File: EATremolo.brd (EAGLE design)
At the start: 54 x 39.4 mm, 34 parts, among them Q1 2N5457, Q2 2N3904, Q3 2N5457, Q4 2N5088

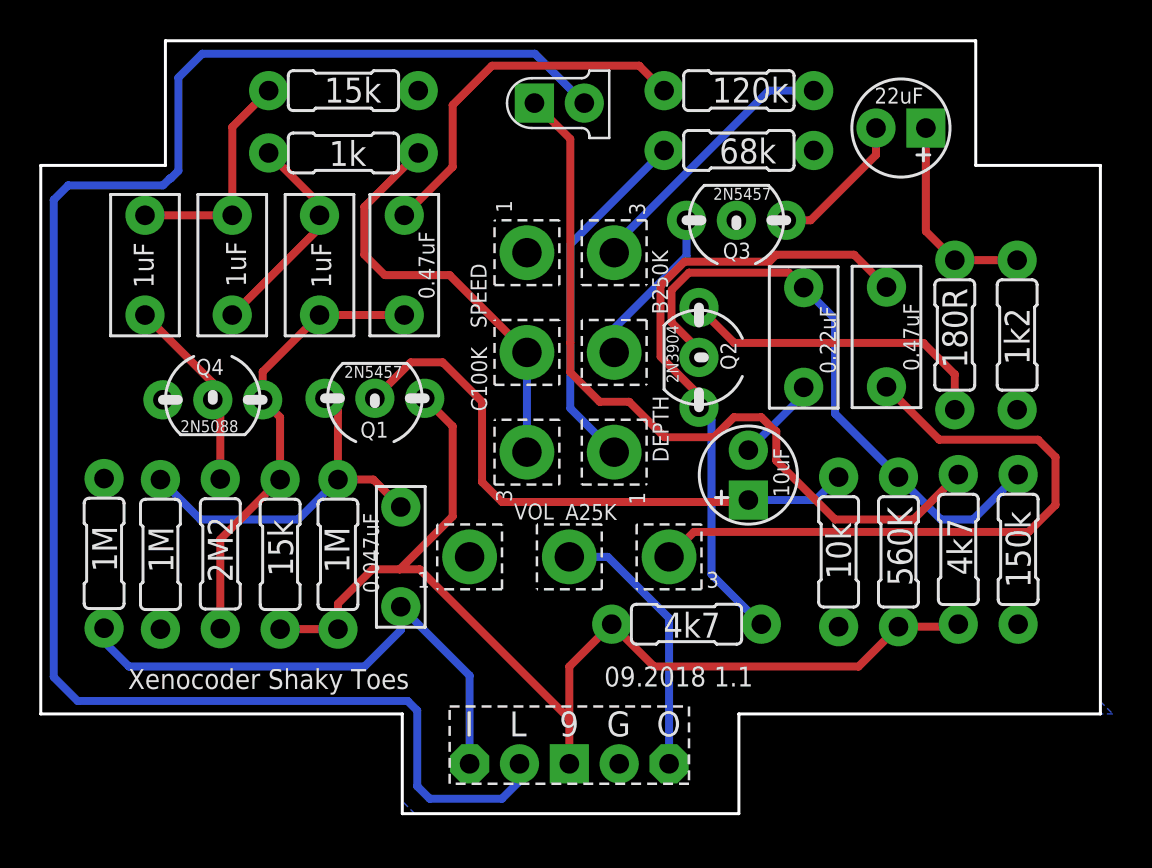
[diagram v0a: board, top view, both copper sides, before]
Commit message: Fixed issue where speed pot was wired (and laid out) backwards
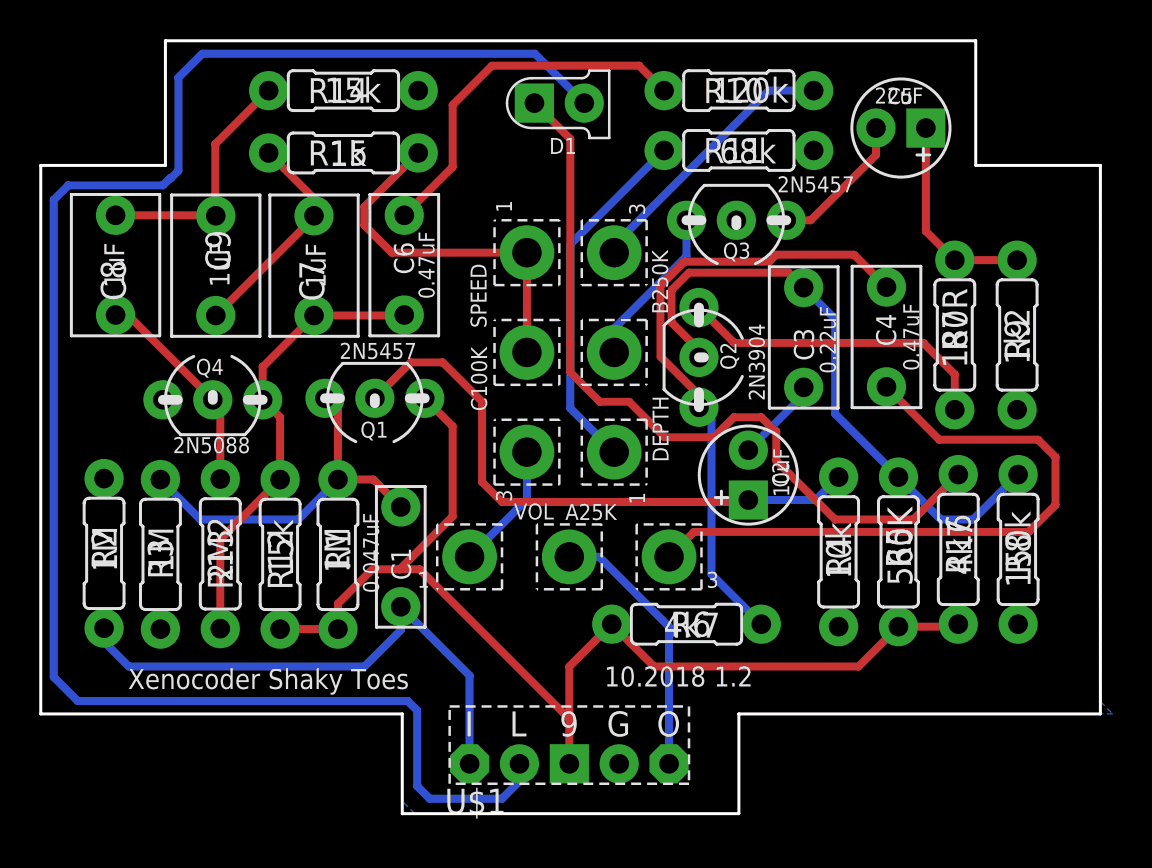
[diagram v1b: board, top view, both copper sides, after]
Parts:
- C7, C8, C9: device mb_caps-box:072X035 -> mb_caps-box:072X045
- moved C8 1.50 mm to (3.81, 27.9)
- moved C9 0.84 mm to (8.92, 27.9)
- moved C7 0.28 mm to (13.9, 27.9)
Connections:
- net GND: now also SPEED.3; no longer SPEED.1
- net N$19: now also SPEED.1; no longer SPEED.3
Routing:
- net GND: track 0.00 -> 6.54 mm
- net N$19: track 21.7 -> 18.8 mm
- net N$18: track 11.6 -> 12.6 mm
- net N$16: track 9.95 -> 10.9 mm
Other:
- board text added: "10.2018 1.2"
- board text removed: "09.2018 1.1"

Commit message: Updated MMBF5457 to right footprint
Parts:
- added U$2, U$3: MMBF5457, xc_library:SOT23
- moved Q3 4.55 mm to (40.0, 30.5)
- moved Q1 3.66 mm to (20.6, 20.5), turned to 90 degrees
- moved Q4 3.00 mm to (5.77, 21.1)
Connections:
- net GND: now also U$3.1
- net N$11: now also U$3.3
- net N$2: now also U$2.3
- net N$22: now also U$2.1
- net N$4: now also U$2.2
- net N$9: now also U$3.2
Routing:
- net GND: track 6.54 -> 17.5 mm
- net N$11: track 8.26 -> 16.4 mm
- net N$2: track 18.9 -> 25.7 mm
- net N$9: track 7.32 -> 13.0 mm
- net N$22: track 57.8 -> 63.0 mm
- net N$15: track 23.3 -> 26.5 mm
- net N$4: track 30.2 -> 28.8 mm

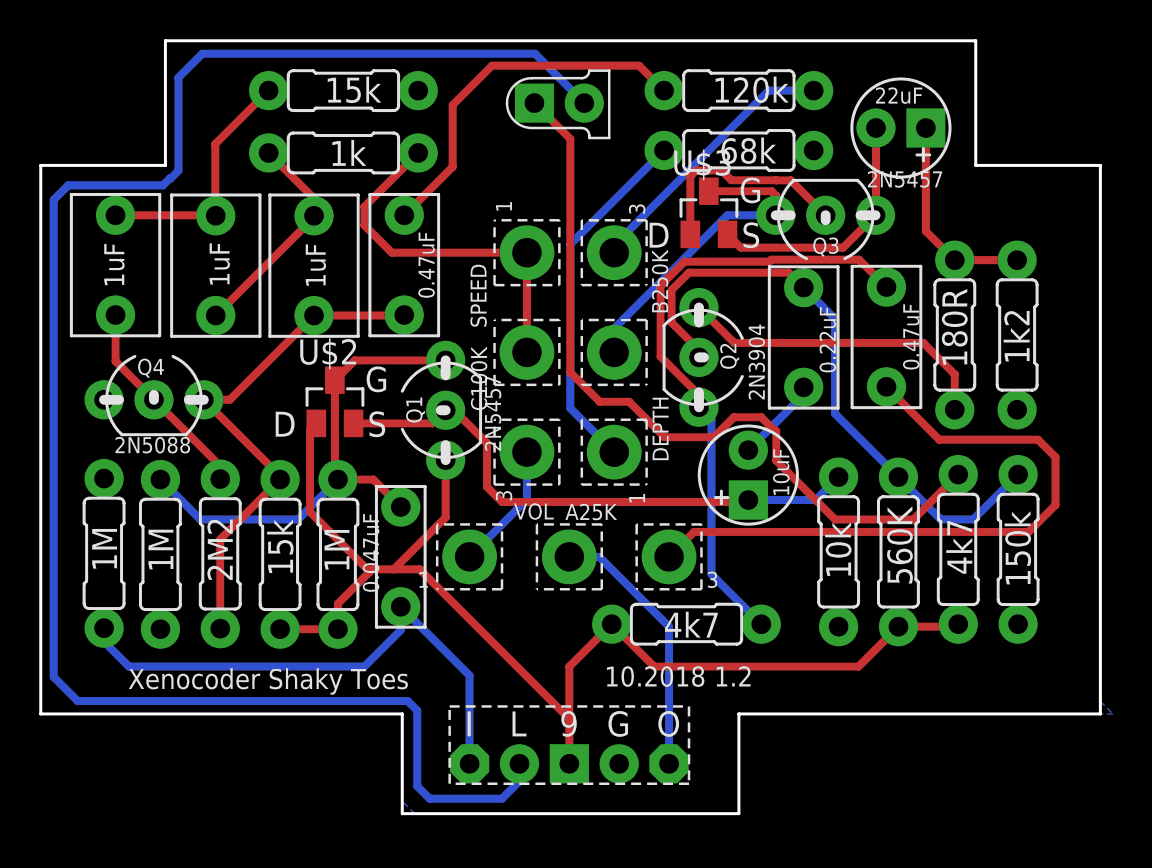
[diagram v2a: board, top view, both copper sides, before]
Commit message: Fixed issue with SMD 5457
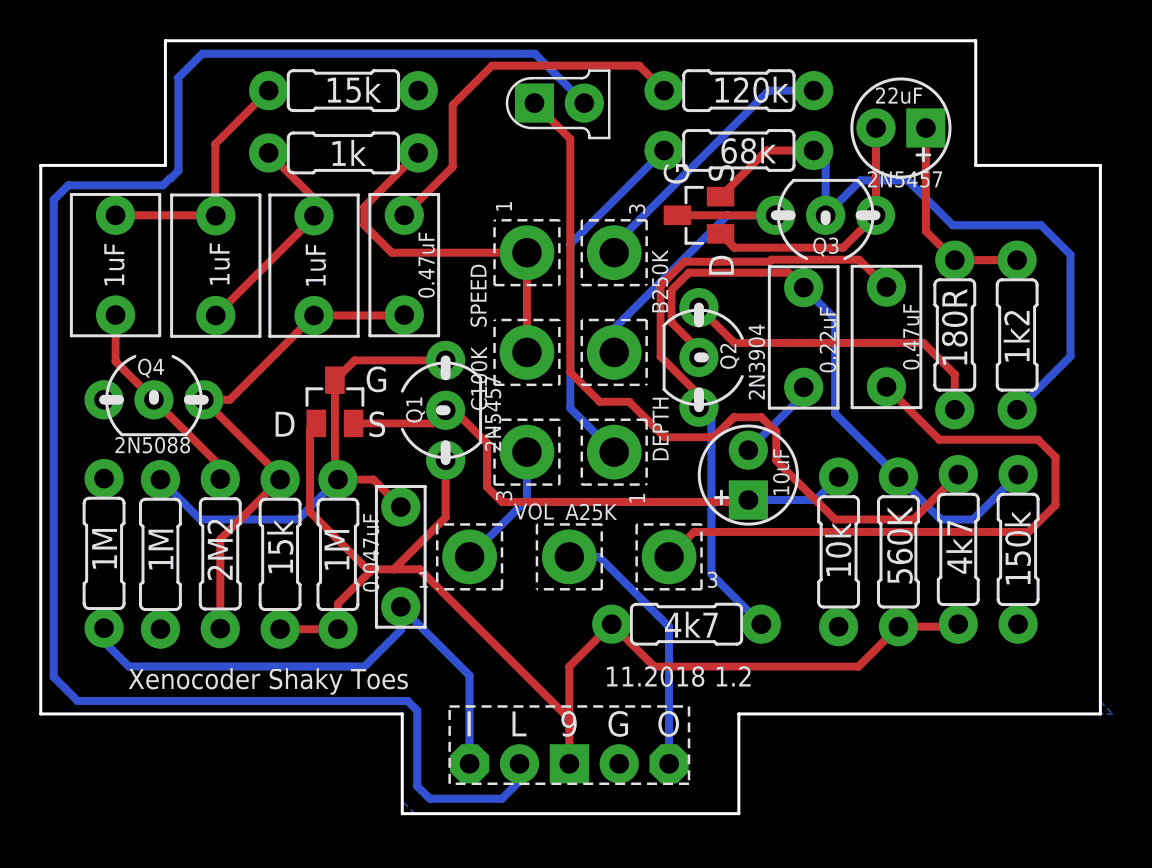
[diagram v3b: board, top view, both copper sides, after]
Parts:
- moved U$3 0.52 mm to (33.5, 30.5), turned to 90 degrees
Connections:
- net GND: now also U$3.2; no longer U$3.1
- net N$9: now also U$3.1; no longer U$3.2
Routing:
- net GND: track 17.5 -> 39.6 mm
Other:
- board text added: "11.2018 1.2"
- board text removed: "10.2018 1.2"
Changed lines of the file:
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@@
 <plain>
 <text x="4.445" y="6.35" size="1.016" layer="25" font="vector">Xenocoder Shaky Toes</text>
-<text x="28.702" y="6.477" size="1.016" layer="25" font="vector">10.2018 1.2</text>
+<text x="28.702" y="6.477" size="1.016" layer="25" font="vector">11.2018 1.2</text>
 <wire x1="0" y1="5.08" x2="18.415" y2="5.08" width="0.1524" layer="20"/>
 <wire x1="18.415" y1="5.08" x2="18.415" y2="0" width="0.1524" layer="20"/>
@@
 <element name="U$1" library="xc_library" package="BOARDLINK" value="BOARDLINK" x="24.384" y="2.54" smashed="yes"/>
 <element name="U$2" library="xc_library" package="SOT23" value="MMBF5457" x="14.986" y="20.9804" smashed="yes">
-<attribute name="NAME" x="13.081" y="22.8854" size="1.27" layer="25"/>
-<attribute name="VALUE" x="13.081" y="17.8054" size="1.27" layer="27"/>
-</element>
-<element name="U$3" library="xc_library" package="SOT23" value="MMBF5457" x="34.036" y="30.607" smashed="yes">
-<attribute name="NAME" x="32.131" y="32.512" size="1.27" layer="25"/>
-<attribute name="VALUE" x="32.131" y="27.432" size="1.27" layer="27"/>
+<attribute name="VALUE" x="10.16" y="22.8854" size="1.27" layer="27"/>
+</element>
+<element name="U$3" library="xc_library" package="SOT23" value="MMBF5457" x="33.528" y="30.48" smashed="yes" rot="R90">
+<attribute name="VALUE" x="32.258" y="32.385" size="1.27" layer="27" rot="R180"/>
 </element>
 </elements>
@@
 <wire x1="21.844" y1="13.081" x2="24.765" y2="16.002" width="0.4064" layer="16"/>
 <wire x1="24.765" y1="16.002" x2="24.765" y2="18.415" width="0.4064" layer="16"/>
-<contactref element="U$3" pad="1"/>
-<wire x1="39.9796" y1="30.48" x2="38.2016" y2="32.258" width="0.4064" layer="1"/>
-<wire x1="38.2016" y1="32.258" x2="37.46786875" y2="32.258" width="0.4064" layer="1"/>
-<wire x1="37.46006875" y1="32.2658" x2="35.179" y2="32.2658" width="0.4064" layer="1"/>
-<wire x1="37.46786875" y1="32.258" x2="37.46006875" y2="32.2658" width="0.4064" layer="1"/>
-<wire x1="34.8916" y1="32.55429375" x2="34.68329375" y2="32.7626" width="0.4064" layer="1"/>
-<wire x1="34.68329375" y1="32.7626" x2="33.38870625" y2="32.7626" width="0.4064" layer="1"/>
-<wire x1="35.179" y1="32.2658" x2="34.8916" y2="32.5532" width="0.4064" layer="1"/>
-<wire x1="34.8916" y1="32.5532" x2="34.8916" y2="32.55429375" width="0.4064" layer="1"/>
-<wire x1="33.38870625" y1="32.7626" x2="33.086" y2="32.45989375" width="0.4064" layer="1"/>
-<wire x1="33.086" y1="32.45989375" x2="33.086" y2="29.507" width="0.4064" layer="1"/>
+<contactref element="U$3" pad="2"/>
+<wire x1="39.9796" y1="30.48" x2="39.9796" y2="33.1724" width="0.4064" layer="16"/>
+<wire x1="39.9796" y1="33.1724" x2="39.37" y2="33.782" width="0.4064" layer="16"/>
+<wire x1="39.9796" y1="30.48" x2="41.7576" y2="32.258" width="0.4064" layer="16"/>
+<wire x1="44.1706" y1="32.258" x2="46.4566" y2="29.972" width="0.4064" layer="16"/>
+<wire x1="50.9524" y1="29.972" x2="52.451" y2="28.4734" width="0.4064" layer="16"/>
+<wire x1="52.451" y1="23.2918" x2="49.7332" y2="20.574" width="0.4064" layer="16"/>
+<wire x1="41.7576" y1="32.258" x2="44.1706" y2="32.258" width="0.4064" layer="16"/>
+<wire x1="46.4566" y1="29.972" x2="50.9524" y2="29.972" width="0.4064" layer="16"/>
+<wire x1="52.451" y1="28.4734" x2="52.451" y2="23.2918" width="0.4064" layer="16"/>
+<wire x1="34.628" y1="31.43" x2="36.98" y2="33.782" width="0.4064" layer="1"/>
+<wire x1="36.98" y1="33.782" x2="39.37" y2="33.782" width="0.4064" layer="1"/>
 </signal>
 <signal name="N$5">
@@
 <contactref element="C5" pad="-"/>
 <contactref element="Q3" pad="3"/>
-<contactref element="U$3" pad="2"/>
 <wire x1="42.545" y1="34.925" x2="42.545" y2="30.5054" width="0.4064" layer="1"/>
 <wire x1="42.545" y1="30.5054" x2="42.5196" y2="30.48" width="0.4064" layer="1"/>
-<wire x1="34.986" y1="29.507" x2="35.664" y2="28.829" width="0.4064" layer="1"/>
+<contactref element="U$3" pad="1"/>
+<wire x1="34.628" y1="29.53" x2="35.329" y2="28.829" width="0.4064" layer="1"/>
 <wire x1="40.8686" y1="28.829" x2="42.5196" y2="30.48" width="0.4064" layer="1"/>
-<wire x1="35.664" y1="28.829" x2="40.8686" y2="28.829" width="0.4064" layer="1"/>
+<wire x1="35.329" y1="28.829" x2="40.8686" y2="28.829" width="0.4064" layer="1"/>
 </signal>
 <signal name="N$14">
@@
 <wire x1="29.21" y1="24.7142" x2="34.9758" y2="30.48" width="0.4064" layer="16"/>
 <contactref element="U$3" pad="3"/>
-<wire x1="34.036" y1="31.707" x2="37.2286" y2="31.707" width="0.4064" layer="1"/>
-<wire x1="37.2286" y1="31.707" x2="37.465" y2="31.4706" width="0.4064" layer="1"/>
-<wire x1="37.465" y1="31.4706" x2="37.4396" y2="31.4452" width="0.4064" layer="1"/>
-<wire x1="37.4396" y1="31.4452" x2="37.4396" y2="30.48" width="0.4064" layer="1"/>
+<wire x1="32.428" y1="30.48" x2="37.4396" y2="30.48" width="0.4064" layer="1"/>
 </signal>
 <signal name="N$12">

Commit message: Version 1.0 of Tremolo Thing
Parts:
- C1: value 0.047uF -> 47nF
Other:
- board text added: "2020.04 v1.0"
- board text added: "Xenocoder Tremolo Thing"
- board text removed: "11.2018 1.2"
- board text removed: "Xenocoder Shaky Toes"
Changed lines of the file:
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@@
 <?xml version="1.0" encoding="utf-8"?>
 <!DOCTYPE eagle SYSTEM "eagle.dtd">
-<eagle version="9.2.2">
+<eagle version="9.5.2">
 <drawing>
 <settings>
@@
 <board>
 <plain>
-<text x="4.445" y="6.35" size="1.016" layer="25" font="vector">Xenocoder Shaky Toes</text>
-<text x="28.702" y="6.477" size="1.016" layer="25" font="vector">11.2018 1.2</text>
+<text x="4.445" y="6.35" size="1.016" layer="25" font="vector">Xenocoder Tremolo Thing</text>
+<text x="28.702" y="6.477" size="1.016" layer="25" font="vector">2020.04 v1.0</text>
 <wire x1="0" y1="5.08" x2="18.415" y2="5.08" width="0.1524" layer="20"/>
 <wire x1="18.415" y1="5.08" x2="18.415" y2="0" width="0.1524" layer="20"/>
@@
 <attribute name="VALUE" x="16.5862" y="34.2646" size="1.27" layer="25" font="vector" ratio="12" rot="R180"/>
 </element>
-<element name="C1" library="mb_caps-box" package="072X025" value="0.047uF" x="18.3388" y="13.081" smashed="yes" rot="R90">
-<attribute name="VALUE" x="17.2306" y="11.234" size="0.8128" layer="25" ratio="12" rot="R90"/>
+<element name="C1" library="mb_caps-box" package="072X025" value="47nF" x="18.3388" y="13.081" smashed="yes" rot="R90">
+<attribute name="VALUE" x="18.2466" y="11.615" size="1.016" layer="25" ratio="12" rot="R90"/>
 </element>
 <element name="C2" library="mb_caps-electro" package="050_020_1" value="10uF" x="36.0426" y="17.2466" smashed="yes" rot="R90">
@@
 <element name="Q1" library="mb_trans" package="TO92-" value="2N5457" x="20.6248" y="20.5486" smashed="yes" rot="R90">
 <attribute name="NAME" x="19.431" y="19.8628" size="0.8128" layer="25" ratio="12" rot="R90"/>
-<attribute name="VALUE" x="23.4442" y="18.415" size="0.8128" layer="25" ratio="12" rot="R90"/>
 </element>
 <element name="Q2" library="mb_trans" package="TO92-" value="2N3904" x="33.528" y="23.241" smashed="yes" rot="R270">
@@
 </element>
 <element name="SPEED" library="mb_pots" package="16MM" value="C100K" x="24.765" y="23.495" smashed="yes" rot="R90">
-<attribute name="NAME" x="22.7076" y="24.7396" size="0.8128" layer="21" ratio="12" rot="R90"/>
-<attribute name="VALUE" x="22.733" y="20.4978" size="0.8128" layer="25" ratio="12" rot="R90"/>
+<attribute name="NAME" x="22.7076" y="27.1526" size="0.8128" layer="21" ratio="12" rot="R90"/>
+<attribute name="VALUE" x="22.733" y="23.2918" size="0.8128" layer="25" ratio="12" rot="R90"/>
 </element>
 <element name="DEPTH" library="mb_pots" package="16MM" value="B250K" x="29.21" y="23.495" smashed="yes" rot="R270">
